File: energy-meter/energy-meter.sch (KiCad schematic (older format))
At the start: 48 parts, among them J1 Screw_Terminal_01x04, J2 Conn_01x03, J3 I2C OLED Display, etc., K1 G5RL-U1A-E, K2 DNP / HF3FF/005-1HST, P1 PineNut, Q1 AP3400, T1 AP-2500, T2 BV 202 0154, T3 DNP / AP-2500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

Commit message: use solid state relays for calibration
That way, we have enough space for two of them. The alternative relay
shares space with the other relay because only one of them will be used.
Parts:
- removed D7: D_Schottky, Diode_SMD:D_SMA_Handsoldering, symbol Device:D_Schottky
- removed Q1: AP3400, Package_TO_SOT_SMD:SOT-23_Handsoldering, symbol Device:Q_NMOS_GSD
- removed R5: 39kOhm, 2W, 1%, Resistor_SMD:R_2512_6332Metric_Pad1.52x3.35mm_HandSolder, symbol Device:R
- removed R8: 10k, Resistor_SMD:R_0603_1608Metric_Pad1.05x0.95mm_HandSolder, symbol Device:R
- removed T3: DNP / AP-2500, energy-meter:AP-2500, symbol energy-meter:AP-2500
- removed TP1, TP2, TP3, TP4, TP5: TestPoint, TestPoint:TestPoint_THTPad_D3.0mm_Drill1.5mm, symbol Connector:TestPoint
- renumbered NT2 to NT1
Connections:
- net labels added: ENA_27k, ENA_470k, L_OUT2
- wire segments 149 -> 140
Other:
- note removed: "alternative use of the 2nd relay:\n- cut L_OUT around TP3\n- TP3 -> through T3 -> TP5\n- N -> TP4\n- L_OUT to external load, as usual\n=> K2 enables internal load"
- note removed: "connect with wire"

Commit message: add opamps
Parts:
- removed D6, D8, D9: ESD5Z5.0T1G, Diode_SMD:D_SOD-523, symbol Device:D_Zener
- removed NT1: Net-Tie_2, NetTie:NetTie-2_SMD_Pad0.5mm, symbol Device:Net-Tie_2
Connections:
- net labels added: BIAS_MCU, CURRENT_OUT0, CURRENT_OUT1, ENA_1000x, ENA_100x, SHORT_CURRENT, TUNE_OFFSET
- net labels removed: DAC0, DAC1, OP1_OUT_F, RELAY2, TEMP1
- wire segments 140 -> 141
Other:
- note added: "DAC"
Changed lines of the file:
@@
 	1    0    0    -1
 $EndComp
-Wire Wire Line
-	1400 1750 1000 1750
-Wire Wire Line
-	1400 1900 1000 1900
-Text Label 1000 1750 0    50   ~ 0
-DAC0
 Text Label 1150 3000 0    50   ~ 0
 SCL
 Text Label 1150 3150 0    50   ~ 0
 SDA
-Text Label 1000 1600 0    50   ~ 0
-TEMP1
-Text Label 950  1450 0    50   ~ 0
-OP1_OUT_F
 Wire Wire Line
 	1150 3150 1400 3150
 Wire Wire Line
 	1400 3000 1150 3000
-Wire Wire Line
-	1000 1600 1400 1600
-Wire Wire Line
-	1400 1450 950  1450
 Text Notes 1850 1850 3    50   ~ 0
 ADC
@@
 Text Label 2300 6550 0    50   ~ 0
 5V
-Text Label 3250 5600 0    50   ~ 0
-SCL
-Text Label 3250 5700 0    50   ~ 0
-SDA
-Text Label 3100 6200 0    50   ~ 0
-TEMP1
-Text Label 3050 6400 0    50   ~ 0
-OP1_OUT_F
-Wire Wire Line
-	3250 5700 3500 5700
-Wire Wire Line
-	3500 5600 3250 5600
-Wire Wire Line
-	3100 6200 3500 6200
-Wire Wire Line
-	3500 6400 3050 6400
 $Comp
 L energy-meter:G5RL-U1A-E K1
@@
 Text GLabel 6750 3250 0    50   Input ~ 0
 N
-Text Label 5050 5950 2    50   ~ 0
+Text Label 5250 5400 2    50   ~ 0
 CURRENT0
-Text Label 5050 6050 2    50   ~ 0
+Text Label 5250 5500 2    50   ~ 0
 CURRENT1
 Wire Wire Line
-	5050 5950 4600 5950
-Wire Wire Line
-	5050 6050 4600 6050
+	5250 5400 4600 5400
+Wire Wire Line
+	5250 5500 4600 5500
 Text Label 8700 2850 0    50   ~ 0
 VOLTAGE0
@@
 Wire Wire Line
 	1400 2550 950  2550
-$Comp
-L power:+3V3 #PWR?
-U 1 1 60A51933
-P 4700 5400
-AR Path="/607B74C2/60A51933" Ref="#PWR?"  Part="1"
-AR Path="/60A51933" Ref="#PWR0108"  Part="1"
-F 0 "#PWR0108" H 4700 5250 50  0001 C CNN
-F 1 "+3V3" V 4715 5528 50  0000 L CNN
-F 2 "" H 4700 5400 50  0001 C CNN
-F 3 "" H 4700 5400 50  0001 C CNN
-	1    4700 5400
-	0    1    1    0
-$EndComp
-Wire Wire Line
-	4600 5400 4700 5400
-$Comp
-L Device:Net-Tie_2 NT1
-U 1 1 60A60821
-P 8150 3550
-F 0 "NT1" H 8150 3500 50  0000 C CNN
-F 1 "Net-Tie_2" H 8150 3640 50  0001 C CNN
-F 2 "NetTie:NetTie-2_SMD_Pad0.5mm" H 8150 3550 50  0001 C CNN
-F 3 "~" H 8150 3550 50  0001 C CNN
-	1    8150 3550
-	1    0    0    -1
-$EndComp
-Text Label 8350 3550 0    50   ~ 0
-BIAS
-Wire Wire Line
-	8350 3550 8250 3550
 $Sheet
 S 3500 5300 1100 2250
@@
 F0 "Modified LCR Meter" 50
 F1 "lcr.sch" 50
-F2 "OP1_OUT_F" I L 3500 6400 50
-F3 "TEMP1" I L 3500 6200 50
-F4 "VDDA" I R 4600 5400 50
-F5 "SCL" I L 3500 5600 50
-F6 "SDA" I L 3500 5700 50
-F7 "CURRENT1" I R 4600 6050 50
-F8 "CURRENT0" I R 4600 5950 50
+F2 "CURRENT1" I R 4600 5500 50
+F3 "CURRENT0" I R 4600 5400 50
+F4 "BIAS_MCU" I R 4600 5650 50
+F5 "TUNE_OFFSET0" I R 4600 5750 50
+F6 "CURRENT_OUT0" I R 4600 5850 50
+F7 "ENA_1000x" I R 4600 6300 50
+F8 "SHORT_CURRENT" I R 4600 6100 50
+F9 "CURRENT_OUT1" I R 4600 5950 50
+F10 "ENA_100x" I R 4600 6200 50
 $EndSheet
-Text Label 1000 1900 0    50   ~ 0
-DAC1
 $Comp
 L energy-meter:L9110S U1
@@
 	9000 2850 8650 2850
 Connection ~ 8650 2850
-$Comp
-L Device:D_Zener D6
-U 1 1 60C5DD5E
-P 9000 3750
-F 0 "D6" V 8954 3829 50  0000 L CNN
-F 1 "ESD5Z5.0T1G" V 9045 3829 50  0000 L CNN
-F 2 "Diode_SMD:D_SOD-523" H 9000 3750 50  0001 C CNN
-F 3 "https://www.onsemi.com/pub/Collateral/ESD5Z2.5T1-D.PDF" H 9000 3750 50  0001 C CNN
-	1    9000 3750
-	0    1    1    0
-$EndComp
-$Comp
-L power:GND #PWR0135
-U 1 1 60C5E7AA
-P 9000 3900
-F 0 "#PWR0135" H 9000 3650 50  0001 C CNN
-F 1 "GND" V 9005 3772 50  0000 R CNN
-F 2 "" H 9000 3900 50  0001 C CNN
-F 3 "" H 9000 3900 50  0001 C CNN
-	1    9000 3900
-	1    0    0    -1
-$EndComp
-Text Label 9000 3600 2    50   ~ 0
-CURRENT0
 Text Label 2850 4700 0    50   ~ 0
 SCL
@@
 Text Label 3500 1350 2    50   ~ 0
 VCC_COIL
-Text Label 1000 1000 0    50   ~ 0
-RELAY2
-Wire Wire Line
-	1000 1000 1400 1000
 $Comp
 L Device:R R?
@@
 	1    0    0    -1
 $EndComp
-Text Label 950  2050 0    50   ~ 0
-CURRENT0
-Wire Wire Line
-	950  2050 1400 2050
-$Comp
-L Device:D_Zener D8
-U 1 1 60E7A9FF
-P 8000 3700
-F 0 "D8" V 7954 3779 50  0000 L CNN
-F 1 "ESD5Z5.0T1G" V 8045 3779 50  0000 L CNN
-F 2 "Diode_SMD:D_SOD-523" H 8000 3700 50  0001 C CNN
-F 3 "https://www.onsemi.com/pub/Collateral/ESD5Z2.5T1-D.PDF" H 8000 3700 50  0001 C CNN
-	1    8000 3700
-	0    1    1    0
-$EndComp
-Wire Wire Line
-	7250 3550 8000 3550
-Wire Wire Line
-	8000 3550 8050 3550
-Connection ~ 8000 3550
-$Comp
-L Device:D_Zener D9
-U 1 1 60E7AE94
-P 8000 4000
-F 0 "D9" V 8046 3921 50  0000 R CNN
-F 1 "ESD5Z5.0T1G" V 7955 3921 50  0000 R CNN
-F 2 "Diode_SMD:D_SOD-523" H 8000 4000 50  0001 C CNN
-F 3 "https://www.onsemi.com/pub/Collateral/ESD5Z2.5T1-D.PDF" H 8000 4000 50  0001 C CNN
-	1    8000 4000
-	0    -1   -1   0
-$EndComp
-Wire Wire Line
-	7250 4150 8000 4150
+Wire Wire Line
+	7250 3550 7950 3550
+Wire Wire Line
+	7250 4150 7950 4150
 Wire Wire Line
 	8300 2850 8050 2850
@@
 Wire Wire Line
 	850  6300 1400 6300
+Text Label 5250 5750 2    50   ~ 0
+TUNE_OFFSET
+Text Label 5250 6100 2    50   ~ 0
+SHORT_CURRENT
+Text Label 5250 6200 2    50   ~ 0
+ENA_100x
+Text Label 5250 6300 2    50   ~ 0
+ENA_1000x
+Text Label 5250 5850 2    50   ~ 0
+CURRENT_OUT0
+Text Label 5250 5950 2    50   ~ 0
+CURRENT_OUT1
+Text Label 5250 5650 2    50   ~ 0
+BIAS_MCU
+Wire Wire Line
+	4600 5650 5250 5650
+Wire Wire Line
+	5250 5750 4600 5750
+Wire Wire Line
+	4600 5850 5250 5850
+Wire Wire Line
+	5250 5950 4600 5950
+Wire Wire Line
+	4600 6100 5250 6100
+Wire Wire Line
+	5250 6200 4600 6200
+Wire Wire Line
+	4600 6300 5250 6300
+Text Label 750  1750 0    50   ~ 0
+TUNE_OFFSET
+Text Label 750  700  0    50   ~ 0
+SHORT_CURRENT
+Text Label 750  1000 0    50   ~ 0
+ENA_100x
+Text Label 750  850  0    50   ~ 0
+ENA_1000x
+Text Label 750  1300 0    50   ~ 0
+CURRENT_OUT0
+Text Label 750  1150 0    50   ~ 0
+CURRENT_OUT1
+Text Notes 1550 1850 0    50   ~ 0
+DAC
+Wire Wire Line
+	750  1750 1400 1750
+Wire Wire Line
+	750  1900 1400 1900
+Wire Wire Line
+	750  1000 1400 1000
+Wire Wire Line
+	1400 850  750  850
+Wire Wire Line
+	750  1150 1400 1150
+Wire Wire Line
+	1400 1300 750  1300
+Wire Wire Line
+	750  700  1400 700
+Text Label 750  1900 0    50   ~ 0
+BIAS_MCU
 $EndSCHEMATC

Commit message: add logos, increase distance to SELV, add PDFs and Gerbers
Lot's of whitespace changes, unfortunately.
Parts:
- added TP3, TP4, TP5, TP6: TestPoint, TestPoint:TestPoint_THTPad_1.0x1.0mm_Drill0.5mm, symbol Connector:TestPoint
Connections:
- wire segments 141 -> 143
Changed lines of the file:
@@
 EESchema Schematic File Version 4
-EELAYER 29 0
+EELAYER 30 0
 EELAYER END
 $Descr A4 11693 8268
@@
 Wire Wire Line
 	8400 3250 8650 3250
-Text Label 9250 850  0    50   ~ 0
+Text Label 8850 850  0    50   ~ 0
 coil-
-Text Label 9250 1550 0    50   ~ 0
+Text Label 8850 1550 0    50   ~ 0
 coil+
 Text GLabel 9950 1550 2    50   Input ~ 0
@@
 Wire Wire Line
 	9900 1550 9950 1550
-Wire Wire Line
-	9250 1550 9500 1550
-Wire Wire Line
-	9250 850  9500 850
 Wire Notes Line
-	9150 600  9150 1650
+	8750 600  8750 1650
 Wire Notes Line
-	11150 600  9150 600
+	11150 600  8750 600
 Wire Notes Line
 	11150 1650 11150 600
 Wire Notes Line
-	9150 1650 11150 1650
+	8750 1650 11150 1650
 Wire Wire Line
 	9500 850  9500 900
@@
 Text Label 750  1900 0    50   ~ 0
 BIAS_MCU
+$Comp
+L Connector:TestPoint TP5
+U 1 1 607FB14D
+P 9200 850
+F 0 "TP5" H 9250 1050 50  0000 R CNN
+F 1 "TestPoint" H 9142 967 50  0001 R CNN
+F 2 "TestPoint:TestPoint_THTPad_1.0x1.0mm_Drill0.5mm" H 9400 850 50  0001 C CNN
+F 3 "~" H 9400 850 50  0001 C CNN
+	1    9200 850
+	-1   0    0    1
+$EndComp
+$Comp
+L Connector:TestPoint TP3
+U 1 1 60807F48
+P 9050 850
+F 0 "TP3" H 9100 1050 50  0000 R CNN
+F 1 "TestPoint" H 8992 967 50  0001 R CNN
+F 2 "TestPoint:TestPoint_THTPad_1.0x1.0mm_Drill0.5mm" H 9250 850 50  0001 C CNN
+F 3 "~" H 9250 850 50  0001 C CNN
+	1    9050 850
+	-1   0    0    1
+$EndComp
+Wire Wire Line
+	9200 850  9500 850
+Wire Wire Line
+	9050 850  8850 850
+$Comp
+L Connector:TestPoint TP6
+U 1 1 6081E7E2
+P 9200 1550
+F 0 "TP6" H 9250 1750 50  0000 R CNN
+F 1 "TestPoint" H 9142 1667 50  0001 R CNN
+F 2 "TestPoint:TestPoint_THTPad_1.0x1.0mm_Drill0.5mm" H 9400 1550 50  0001 C CNN
+F 3 "~" H 9400 1550 50  0001 C CNN
+	1    9200 1550
+	1    0    0    -1
+$EndComp
+$Comp
+L Connector:TestPoint TP4
+U 1 1 6081F0D0
+P 9050 1550
+F 0 "TP4" H 9100 1750 50  0000 R CNN
+F 1 "TestPoint" H 8992 1667 50  0001 R CNN
+F 2 "TestPoint:TestPoint_THTPad_1.0x1.0mm_Drill0.5mm" H 9250 1550 50  0001 C CNN
+F 3 "~" H 9250 1550 50  0001 C CNN
+	1    9050 1550
+	1    0    0    -1
+$EndComp
+Wire Wire Line
+	9200 1550 9500 1550
+Wire Wire Line
+	8850 1550 9050 1550
 $EndSCHEMATC

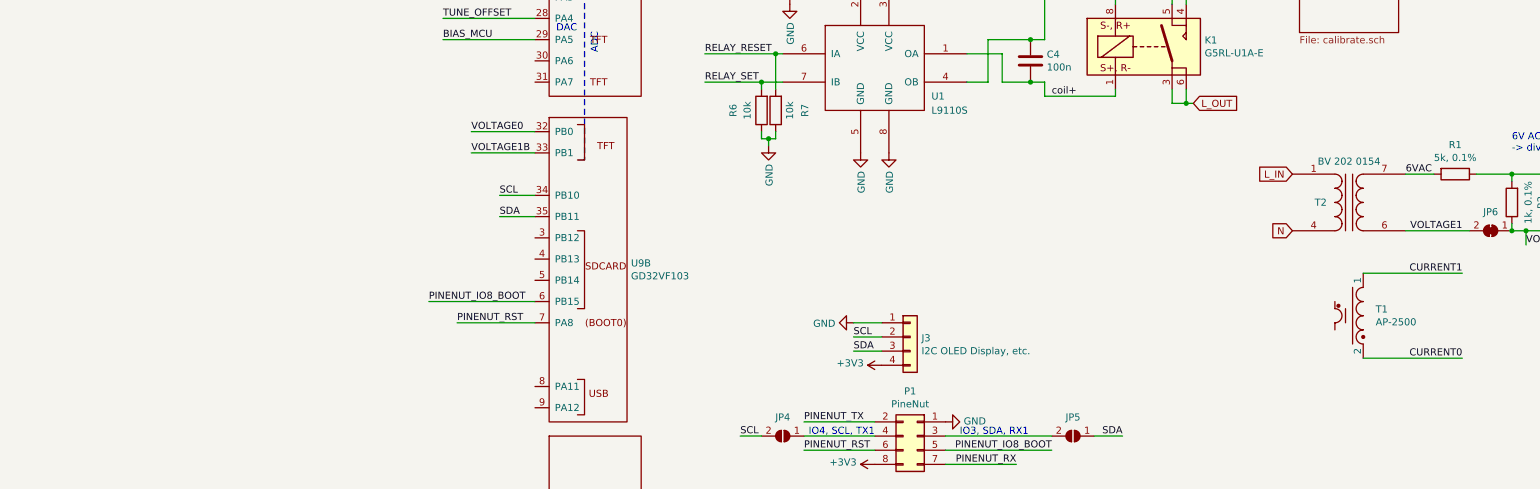
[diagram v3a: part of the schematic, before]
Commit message: open files on Windows, add comment
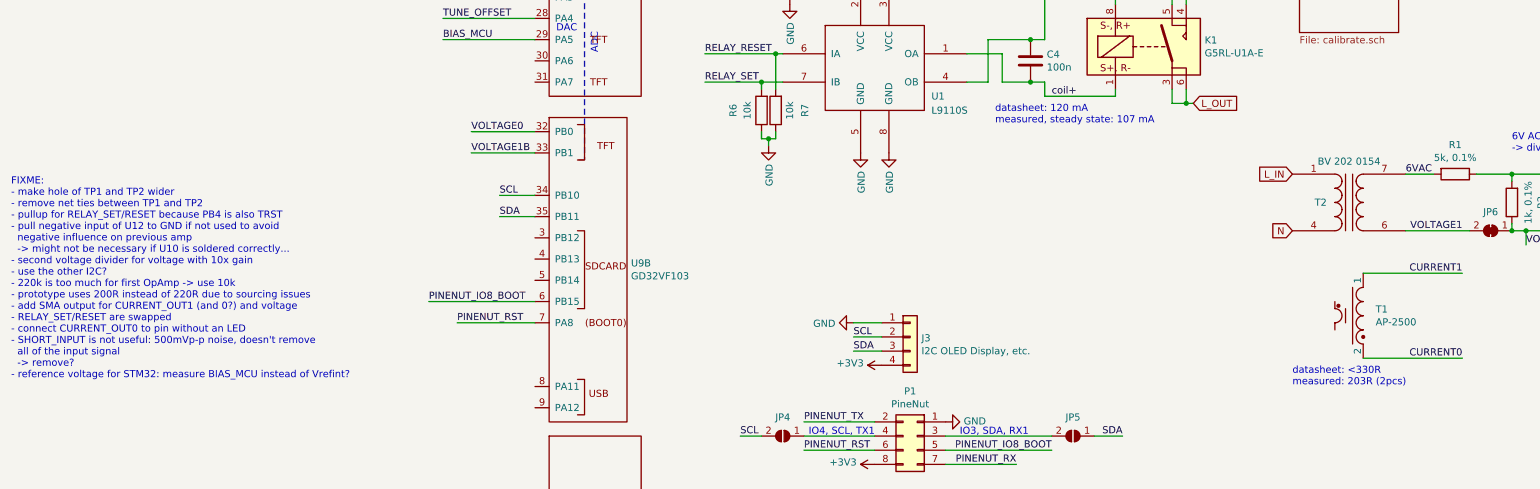
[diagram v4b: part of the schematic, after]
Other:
- note added: "FIXME:\n- make hole of TP1 and TP2 wider\n- remove net ties between TP1 and TP2\n- pullup for RELAY_SET/RESET because PB4 is also TRST\n- pull negative input of U12 to GND if not used to avoid\n negative influence on previous amp\n -> might not be necessary if U10 is soldered correctly...\n- second voltage divider for voltage with 10x gain\n- use the other I2C?\n- 220k is too much for first OpAmp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"
- note added: "datasheet: 120 mA\nmeasured, steady state: 107 mA"
- note added: "datasheet: <330R\nmeasured: 203R (2pcs)"
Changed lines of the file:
@@
 EESchema Schematic File Version 4
-EELAYER 30 0
+LIBS:energy-meter-cache
+EELAYER 29 0
 EELAYER END
 $Descr A4 11693 8268
@@
 Wire Wire Line
 	8850 1550 9050 1550
+Text Notes -2300 4300 0    50   ~ 0
+FIXME:\n- make hole of TP1 and TP2 wider\n- remove net ties between TP1 and TP2\n- pullup for RELAY_SET/RESET because PB4 is also TRST\n- pull negative input of U12 to GND if not used to avoid\n  negative influence on previous amp\n  -> might not be necessary if U10 is soldered correctly...\n- second voltage divider for voltage with 10x gain\n- use the other I2C?\n- 220k is too much for first OpAmp -> use 10k\n- prototype uses 200R instead of 220R due to sourcing issues\n- add SMA output for CURRENT_OUT1 (and 0?) and voltage\n- RELAY_SET/RESET are swapped\n- connect CURRENT_OUT0 to pin without an LED\n- SHORT_INPUT is not useful: 500mVp-p noise, doesn't remove\n  all of the input signal\n  -> remove?\n- reference voltage for STM32: measure BIAS_MCU instead of Vrefint?
+Text Notes 4650 2500 0    50   ~ 0
+datasheet: 120 mA\nmeasured, steady state: 107 mA
+Text Notes 6750 4350 0    50   ~ 0
+datasheet: <330R\nmeasured: 203R (2pcs)
 $EndSCHEMATC

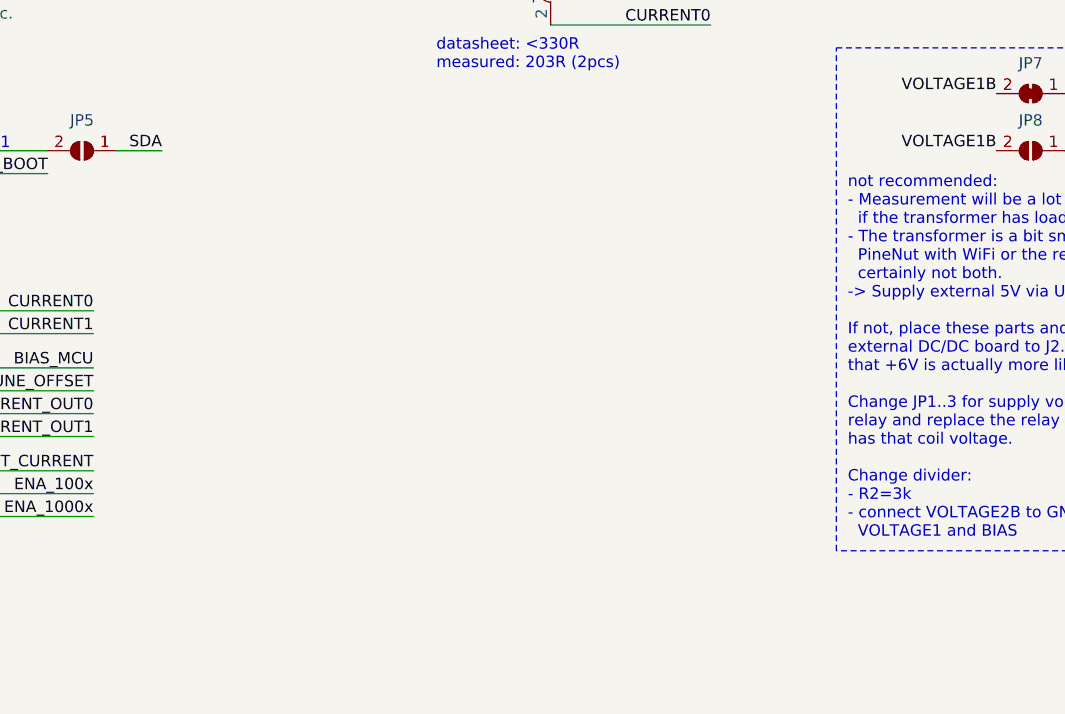
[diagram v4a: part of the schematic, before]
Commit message: add sheet with warnings and design info
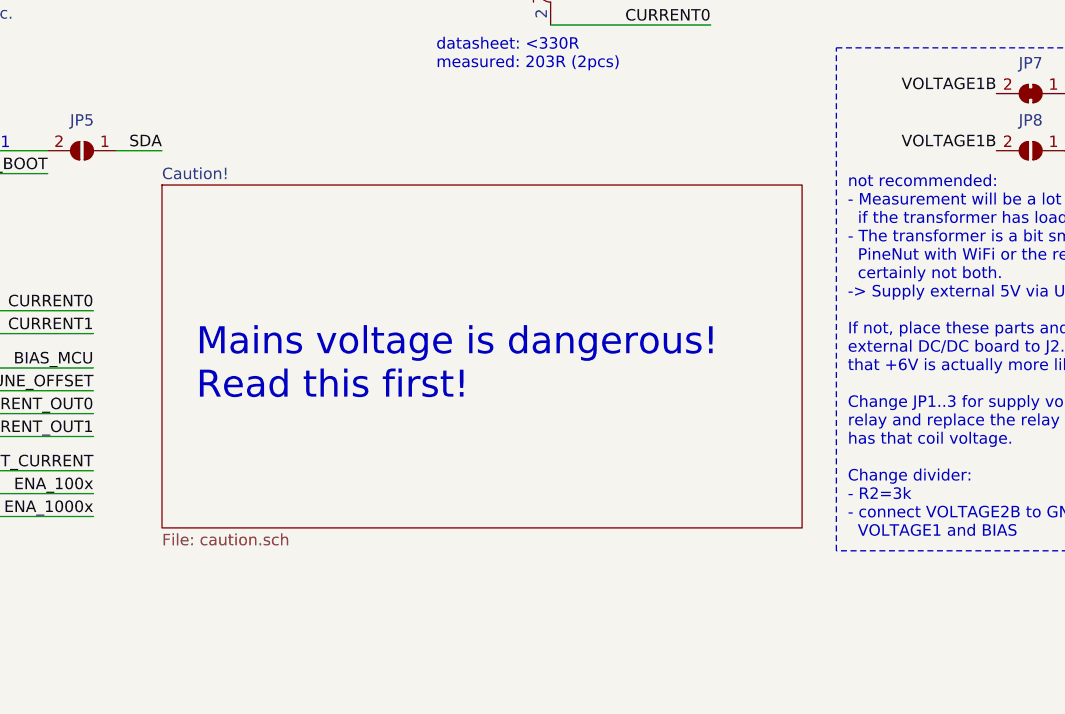
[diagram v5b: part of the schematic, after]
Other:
- note added: "Mains voltage is dangerous!\nRead this first!"
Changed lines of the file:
@@
 $Descr A4 11693 8268
 encoding utf-8
-Sheet 1 3
+Sheet 1 4
 Title ""
 Date ""
@@
 Text Notes 6750 4350 0    50   ~ 0
 datasheet: <330R\nmeasured: 203R (2pcs)
+$Sheet
+S 5550 4850 2800 1500
+U 60C0852B
+F0 "Caution!" 50
+F1 "caution.sch" 50
+$EndSheet
+Text Notes 5700 5800 0    118  ~ 0
+Mains voltage is dangerous!\nRead this first!
 $EndSCHEMATC

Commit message: remove optional parts, increase distance between conductors on primary side
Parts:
- removed K2: DNP / HF3FF/005-1HST, energy-meter:Relay_HF3FF_005, symbol Relay:DIPxx-1Axx-11x
- removed TP3, TP4, TP5, TP6: TestPoint, TestPoint:TestPoint_THTPad_1.0x1.0mm_Drill0.5mm, symbol Connector:TestPoint
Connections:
- wire segments 143 -> 133
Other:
- note removed: "alternative relay:\ncheap but not bistable"
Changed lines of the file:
@@
 Wire Wire Line
 	8400 3250 8650 3250
-Text Label 8850 850  0    50   ~ 0
-coil-
-Text Label 8850 1550 0    50   ~ 0
-coil+
-Text GLabel 9950 1550 2    50   Input ~ 0
-L_OUT
-Text GLabel 9950 850  2    50   Input ~ 0
-L_IN
-Wire Wire Line
-	9900 1550 9950 1550
-Wire Notes Line
-	8750 600  8750 1650
-Wire Notes Line
-	11150 600  8750 600
-Wire Notes Line
-	11150 1650 11150 600
-Wire Notes Line
-	8750 1650 11150 1650
-Wire Wire Line
-	9500 850  9500 900
-Wire Wire Line
-	9500 1550 9500 1500
-Text Notes 10200 1400 0    50   ~ 0
-alternative relay:\ncheap but not bistable
-Wire Wire Line
-	9900 1550 9900 1500
-Wire Wire Line
-	9900 850  9900 900
-Wire Wire Line
-	9950 850  9900 850
-$Comp
-L Relay:DIPxx-1Axx-11x K2
-U 1 1 60CDDACF
-P 9700 1200
-F 0 "K2" H 10050 1350 50  0000 L CNN
-F 1 "DNP / HF3FF/005-1HST" H 10050 1250 50  0000 L CNN
-F 2 "energy-meter:Relay_HF3FF_005" H 10050 1150 50  0001 L CNN
-F 3 "https://standexelectronics.com/wp-content/uploads/datasheet_reed_relay_DIP.pdf" H 9700 1200 50  0001 C CNN
-F 4 "https://www.tme.eu/de/details/hf3ff_005-1hst/elektromagnetische-mini-relais/hongfa-relay/" H 9700 1200 50  0001 C CNN "TME"
-	1    9700 1200
-	1    0    0    -1
-$EndComp
 $Sheet
 S 6800 650  700  1200
@@
 Text Label 750  1900 0    50   ~ 0
 BIAS_MCU
-$Comp
-L Connector:TestPoint TP5
-U 1 1 607FB14D
-P 9200 850
-F 0 "TP5" H 9250 1050 50  0000 R CNN
-F 1 "TestPoint" H 9142 967 50  0001 R CNN
-F 2 "TestPoint:TestPoint_THTPad_1.0x1.0mm_Drill0.5mm" H 9400 850 50  0001 C CNN
-F 3 "~" H 9400 850 50  0001 C CNN
-	1    9200 850
-	-1   0    0    1
-$EndComp
-$Comp
-L Connector:TestPoint TP3
-U 1 1 60807F48
-P 9050 850
-F 0 "TP3" H 9100 1050 50  0000 R CNN
-F 1 "TestPoint" H 8992 967 50  0001 R CNN
-F 2 "TestPoint:TestPoint_THTPad_1.0x1.0mm_Drill0.5mm" H 9250 850 50  0001 C CNN
-F 3 "~" H 9250 850 50  0001 C CNN
-	1    9050 850
-	-1   0    0    1
-$EndComp
-Wire Wire Line
-	9200 850  9500 850
-Wire Wire Line
-	9050 850  8850 850
-$Comp
-L Connector:TestPoint TP6
-U 1 1 6081E7E2
-P 9200 1550
-F 0 "TP6" H 9250 1750 50  0000 R CNN
-F 1 "TestPoint" H 9142 1667 50  0001 R CNN
-F 2 "TestPoint:TestPoint_THTPad_1.0x1.0mm_Drill0.5mm" H 9400 1550 50  0001 C CNN
-F 3 "~" H 9400 1550 50  0001 C CNN
-	1    9200 1550
-	1    0    0    -1
-$EndComp
-$Comp
-L Connector:TestPoint TP4
-U 1 1 6081F0D0
-P 9050 1550
-F 0 "TP4" H 9100 1750 50  0000 R CNN
-F 1 "TestPoint" H 8992 1667 50  0001 R CNN
-F 2 "TestPoint:TestPoint_THTPad_1.0x1.0mm_Drill0.5mm" H 9250 1550 50  0001 C CNN
-F 3 "~" H 9250 1550 50  0001 C CNN
-	1    9050 1550
-	1    0    0    -1
-$EndComp
-Wire Wire Line
-	9200 1550 9500 1550
-Wire Wire Line
-	8850 1550 9050 1550
 Text Notes -2300 4300 0    50   ~ 0
 FIXME:\n- make hole of TP1 and TP2 wider\n- remove net ties between TP1 and TP2\n- pullup for RELAY_SET/RESET because PB4 is also TRST\n- pull negative input of U12 to GND if not used to avoid\n  negative influence on previous amp\n  -> might not be necessary if U10 is soldered correctly...\n- second voltage divider for voltage with 10x gain\n- use the other I2C?\n- 220k is too much for first OpAmp -> use 10k\n- prototype uses 200R instead of 220R due to sourcing issues\n- add SMA output for CURRENT_OUT1 (and 0?) and voltage\n- RELAY_SET/RESET are swapped\n- connect CURRENT_OUT0 to pin without an LED\n- SHORT_INPUT is not useful: 500mVp-p noise, doesn't remove\n  all of the input signal\n  -> remove?\n- reference voltage for STM32: measure BIAS_MCU instead of Vrefint?
